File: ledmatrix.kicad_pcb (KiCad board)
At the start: 4 copper layers, 49.8 x 83.2 mm, 86 parts, among them J1 Conn_02x06_Odd_Even, J2 Conn_02x06_Odd_Even, J3 Conn_01x02, Q1 BSS84, Q2 BSS84, Q3 BSS84, Q4 BSS84, Q5 BSS84, Q6 BSS84, Q7 BSS84, Q8 BSS84, U1 mbi5029gd, U2 74HC137

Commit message: nicefy
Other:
- board text added: "'HC137 (rows)"
- board text added: "A -- K green A -- K red"
- board text added: "A1 A0 ~{E1} A2 CLK LE ~{OE} DIN ⏚ ⏚ 5V 5V"
- board text added: "A1 A0 ~{E1} A2 CLK LE ~{OE} DOUT ⏚ ⏚ 5V 5V"
- board text added: "green = col 14 ↑ red = col 15 ↑"
- board text added: "mbi5029gd (cols)"
- board text added: "↑ green = col 0 ↑ red = col 1"
- board text added: "↓ row 0 ↓"
- board text added: "↓ row 7 ↓"
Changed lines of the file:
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@@
   (net 42 "/A6")
   (net 43 "/A7")
-  (net 44 "Net-(U1-Pad23)")
+  (net 44 "Net-(R1-Pad2)")
   (footprint "panasonic_led_ln2162c68:LN2162C68" (layer "F.Cu")
     (at 90.17 95.25)
@@
       (net 18 "+5V") (pintype "passive"))
     (pad "2" smd roundrect locked (at 0.825 0 90) (size 0.8 0.95) (layers "F.Cu" "F.Paste" "F.Mask") (roundrect_rratio 0.25)
-      (net 44 "Net-(U1-Pad23)") (pintype "passive"))
+      (net 44 "Net-(R1-Pad2)") (pintype "passive"))
     (model "${KICAD6_3DMODEL_DIR}/Resistor_SMD.3dshapes/R_0603_1608Metric.wrl"
       (offset (xyz 0 0 0))
@@
       (net 35 "/DOUT") (pinfunction "SDO") (pintype "output"))
     (pad "23" smd roundrect locked (at 4.65 -5.715 90) (size 2.05 0.6) (layers "F.Cu" "F.Paste" "F.Mask") (roundrect_rratio 0.25)
-      (net 44 "Net-(U1-Pad23)") (pinfunction "R-EXT") (pintype "passive"))
+      (net 44 "Net-(R1-Pad2)") (pinfunction "R-EXT") (pintype "passive"))
     (pad "24" smd roundrect locked (at 4.65 -6.985 90) (size 2.05 0.6) (layers "F.Cu" "F.Paste" "F.Mask") (roundrect_rratio 0.25)
       (net 18 "+5V") (pinfunction "VDD") (pintype "power_in"))
@@
     (property "Sheetname" "")
     (attr smd)
-    (fp_text reference "C1" (at 1.905 -3.048 180) (layer "F.SilkS")
+    (fp_text reference "C1" (at 2.286 1.524 180) (layer "F.SilkS")
       (effects (font (size 0.75 0.75) (thickness 0.1)))
     )
@@
     (fp_line (start -1.93 -8.4) (end -3.13 -8.4) (layer "B.Fab") (width 0.1))
     (pad "1" thru_hole roundrect locked (at 0 0 180) (size 1.7 1.7) (drill 1) (layers *.Cu *.Mask) (roundrect_rratio 0.1470588235)
-      (net 26 "/ROW_A0") (pinfunction "Pin_1") (pintype "passive"))
+      (net 26 "/ROW_A0") (pinfunction "Pin_1"))
     (pad "2" thru_hole circle locked (at 2.54 0 180) (size 1.7 1.7) (drill 1) (layers *.Cu *.Mask)
-      (net 31 "/ROW_A1") (pinfunction "Pin_2") (pintype "passive"))
+      (net 31 "/ROW_A1") (pinfunction "Pin_2"))
     (pad "3" thru_hole circle locked (at 0 -2.54 180) (size 1.7 1.7) (drill 1) (layers *.Cu *.Mask)
-      (net 27 "/ROW_A2") (pinfunction "Pin_3") (pintype "passive"))
+      (net 27 "/ROW_A2") (pinfunction "Pin_3"))
     (pad "4" thru_hole circle locked (at 2.54 -2.54 180) (size 1.7 1.7) (drill 1) (layers *.Cu *.Mask)
-      (net 32 "/ROW_~{E1}") (pinfunction "Pin_4") (pintype "passive"))
+      (net 32 "/ROW_~{E1}") (pinfunction "Pin_4"))
     (pad "5" thru_hole circle locked (at 0 -5.08 180) (size 1.7 1.7) (drill 1) (layers *.Cu *.Mask)
-      (net 28 "/LE{slash}MOD{slash}CA") (pinfunction "Pin_5") (pintype "passive"))
+      (net 28 "/LE{slash}MOD{slash}CA") (pinfunction "Pin_5"))
     (pad "6" thru_hole circle locked (at 2.54 -5.08 180) (size 1.7 1.7) (drill 1) (layers *.Cu *.Mask)
-      (net 33 "/CLK") (pinfunction "Pin_6") (pintype "passive"))
+      (net 33 "/CLK") (pinfunction "Pin_6"))
     (pad "7" thru_hole circle locked (at 0 -7.62 180) (size 1.7 1.7) (drill 1) (layers *.Cu *.Mask)
-      (net 29 "/DIN") (pinfunction "Pin_7") (pintype "passive"))
+      (net 29 "/DIN") (pinfunction "Pin_7"))
     (pad "8" thru_hole circle locked (at 2.54 -7.62 180) (size 1.7 1.7) (drill 1) (layers *.Cu *.Mask)
-      (net 34 "/~{OE}{slash}SW{slash}~{ED}") (pinfunction "Pin_8") (pintype "passive"))
+      (net 34 "/~{OE}{slash}SW{slash}~{ED}") (pinfunction "Pin_8"))
     (pad "9" thru_hole circle locked (at 0 -10.16 180) (size 1.7 1.7) (drill 1) (layers *.Cu *.Mask)
-      (net 30 "GND") (pinfunction "Pin_9") (pintype "passive"))
+      (net 30 "GND") (pinfunction "Pin_9"))
     (pad "10" thru_hole circle locked (at 2.54 -10.16 180) (size 1.7 1.7) (drill 1) (layers *.Cu *.Mask)
-      (net 30 "GND") (pinfunction "Pin_10") (pintype "passive"))
+      (net 30 "GND") (pinfunction "Pin_10"))
     (pad "11" thru_hole circle locked (at 0 -12.7 180) (size 1.7 1.7) (drill 1) (layers *.Cu *.Mask)
-      (net 18 "+5V") (pinfunction "Pin_11") (pintype "passive"))
+      (net 18 "+5V") (pinfunction "Pin_11"))
     (pad "12" thru_hole circle locked (at 2.54 -12.7 180) (size 1.7 1.7) (drill 1) (layers *.Cu *.Mask)
-      (net 18 "+5V") (pinfunction "Pin_12") (pintype "passive"))
+      (net 18 "+5V") (pinfunction "Pin_12"))
     (model "${KICAD6_3DMODEL_DIR}/Connector_IDC.3dshapes/IDC-Header_2x06_P2.54mm_Latch_Vertical.wrl"
       (offset (xyz 0 0 0))
@@
     )
   )
+  (gr_line (start 91.186 25.908) (end 90.932 26.162) (layer "F.SilkS") (width 0.127))
+  (gr_line (start 90.932 24.511) (end 90.678 24.511) (layer "F.SilkS") (width 0.127))
+  (gr_line (start 91.186 23.876) (end 90.932 24.13) (layer "F.SilkS") (width 0.127))
+  (gr_line (start 90.932 25.654) (end 91.186 25.908) (layer "F.SilkS") (width 0.127))
+  (gr_line (start 90.932 22.86) (end 90.932 23.622) (layer "F.SilkS") (width 0.127))
+  (gr_line (start 90.932 23.622) (end 91.186 23.876) (layer "F.SilkS") (width 0.127))
+  (gr_line (start 90.932 24.13) (end 90.932 24.511) (layer "F.SilkS") (width 0.127))
+  (gr_line (start 90.932 27.178) (end 90.678 27.178) (layer "F.SilkS") (width 0.127))
+  (gr_line (start 90.932 26.162) (end 90.932 27.178) (layer "F.SilkS") (width 0.127))
+  (gr_line (start 90.678 22.86) (end 90.932 22.86) (layer "F.SilkS") (width 0.127))
+  (gr_line (start 90.678 24.892) (end 90.932 24.892) (layer "F.SilkS") (width 0.127))
+  (gr_line (start 90.932 24.892) (end 90.932 25.654) (layer "F.SilkS") (width 0.127))
   (gr_line (start 118.245 104.267) (end 68.445 104.267) (layer "Edge.Cuts") (width 0.1))
   (gr_line (start 68.445 104.267) (end 68.445 21.082) (layer "Edge.Cuts") (width 0.1))
   (gr_line (start 118.245 21.082) (end 118.245 104.267) (layer "Edge.Cuts") (width 0.1))
   (gr_line (start 118.245 21.082) (end 68.445 21.082) (layer "Edge.Cuts") (width 0.1))
+  (gr_text "↓ row 0 ↓" (at 83.82 54.356) (layer "F.SilkS")
+    (effects (font (size 0.75 0.75) (thickness 0.1)))
+  )
+  (gr_text "'HC137\n(rows)" (at 94.488 23.876) (layer "F.SilkS")
+    (effects (font (size 0.75 0.75) (thickness 0.1)))
+  )
+  (gr_text "↑ green = col 0\n↑ red = col 1" (at 70.612 66.548) (layer "F.SilkS")
+    (effects (font (size 0.75 0.75) (thickness 0.1)) (justify left))
+  )
+  (gr_text "mbi5029gd\n(cols)" (at 94.488 26.924) (layer "F.SilkS")
+    (effects (font (size 0.75 0.75) (thickness 0.1)))
+  )
+  (gr_text "green = col 14 ↑\nred = col 15 ↑" (at 115.57 66.548) (layer "F.SilkS")
+    (effects (font (size 0.75 0.75) (thickness 0.1)) (justify right))
+  )
+  (gr_text "A1 A0\n~{E1} A2\nCLK LE\n~{OE} DOUT\n⏚ ⏚\n5V 5V" (at 87.63 26.162) (layer "F.SilkS")
+    (effects (font (size 0.75 0.75) (thickness 0.1)))
+  )
+  (gr_text "↓ row 7 ↓" (at 83.82 98.552) (layer "F.SilkS")
+    (effects (font (size 0.75 0.75) (thickness 0.1)))
+  )
+  (gr_text "A -- K green\nA -- K red" (at 94.234 60.325) (layer "F.SilkS")
+    (effects (font (size 0.75 0.75) (thickness 0.1)) (justify left))
+  )
+  (gr_text "A1 A0\n~{E1} A2\nCLK LE\n~{OE} DIN\n⏚ ⏚\n5V 5V" (at 74.93 26.162) (layer "F.SilkS")
+    (effects (font (size 0.75 0.75) (thickness 0.1)))
+  )
   (segment (start 105.41 52.578) (end 105.664 52.324) (width 0.127) (layer "F.Cu") (net 1))
   (segment (start 72.82 59.612) (end 72.82 62.6) (width 0.127) (layer "F.Cu") (net 1))

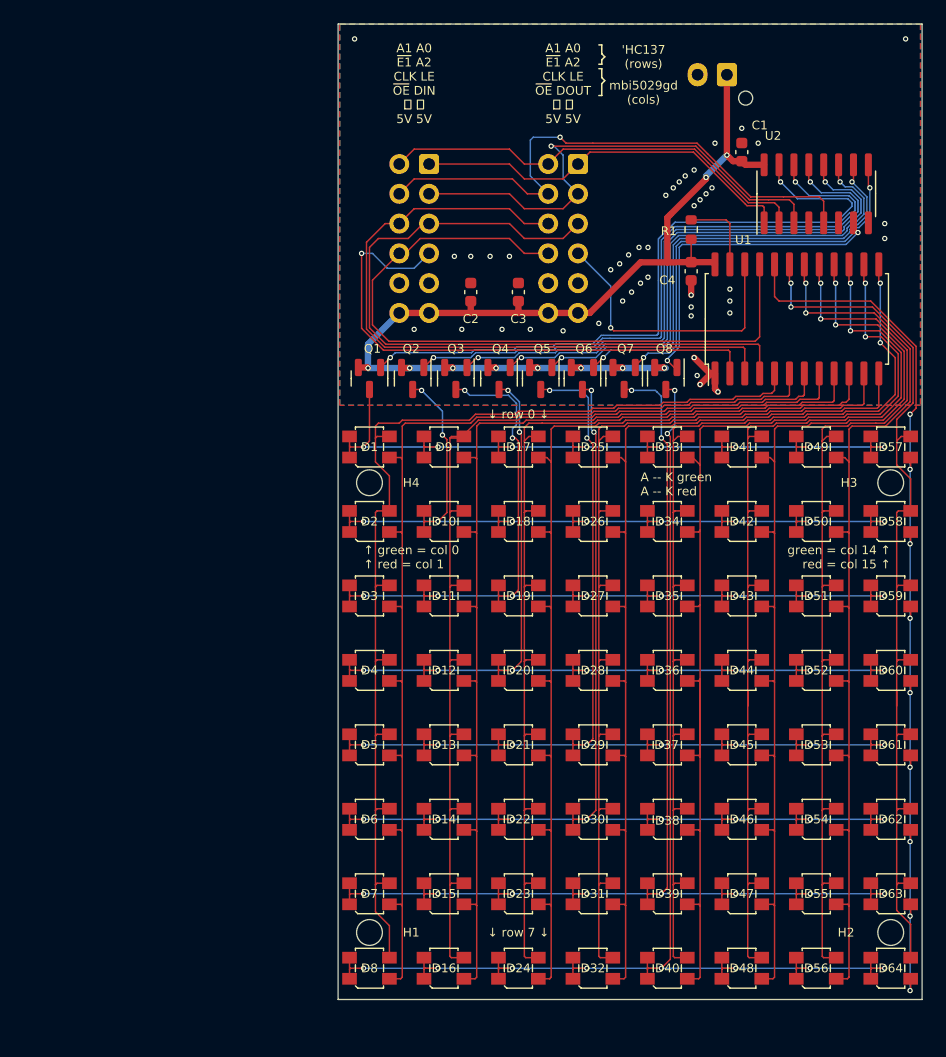
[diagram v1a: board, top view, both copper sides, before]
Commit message: changes, mostly adapting to proper JLCpcb 4layer rules
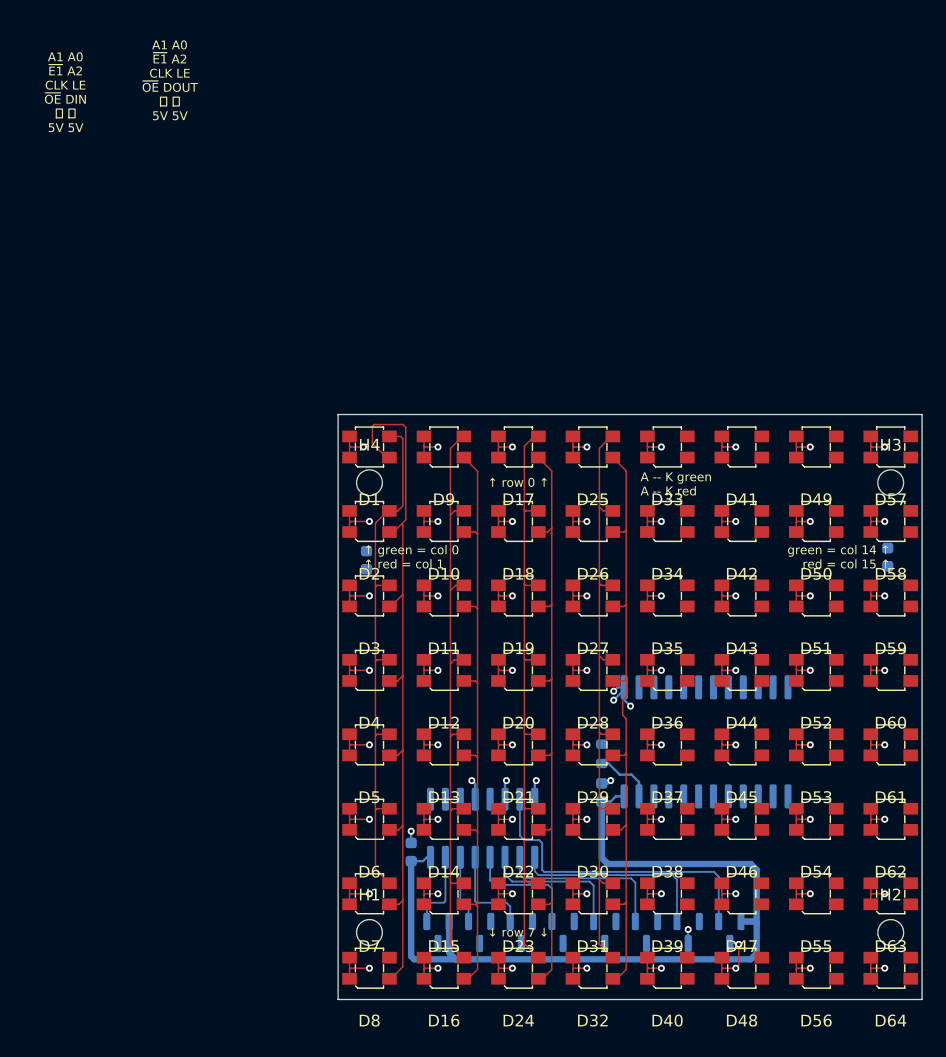
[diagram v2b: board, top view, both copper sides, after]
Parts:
- removed J1, J2: Conn_02x06_Odd_Even, Connector_IDC:IDC-Header_2x06_P2.54mm_Latch_Vertical
- removed J3: Conn_01x02, Connector_JST:JST_XH_B2B-XH-AM_1x02_P2.50mm_Vertical
- C1, C2, C3, C4, Q1, Q2, Q3, Q4, Q5, Q6, Q7, Q8, R1, U1, U2: moved to B.Cu
- moved C1 66.0 mm to (74.7, 91.7)
- moved U2 61.1 mm to (80.8, 89.7), turned to -90 degrees
- moved Q1 47.6 mm to (77.0, 98.6)
- moved Q2 47.6 mm to (80.5, 98.6)
- moved Q3 47.6 mm to (84.1, 98.6)
- moved Q4 47.6 mm to (87.6, 98.6)
- moved Q5 47.6 mm to (91.2, 98.6)
- moved Q6 47.6 mm to (94.7, 98.6)
- moved Q7 47.6 mm to (98.3, 98.6)
- moved Q8 47.6 mm to (101.9, 98.6)
- moved R1 45.3 mm to (90.9, 83.3), turned to -90 degrees
- moved C4 45.1 mm to (90.9, 86.6), turned to 90 degrees
- moved C2 42.1 mm to (115.3, 66.5)
- moved U1 36.9 mm to (99.8, 82.3), turned to -90 degrees
- moved C3 26.3 mm to (70.9, 66.8)
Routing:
- net /LED Matrix/K9: track 94.0 -> 0.00 mm, vias 2 -> 0
- net /LED Matrix/K8: track 86.9 -> 0.00 mm, vias 2 -> 0
- net /LED Matrix/K10: track 84.9 -> 0.00 mm, vias 2 -> 0
- net /LED Matrix/K11: track 84.2 -> 0.00 mm, vias 2 -> 0
- net /LED Matrix/K13: track 81.0 -> 0.00 mm, vias 2 -> 0
- net /LED Matrix/K12: track 80.8 -> 0.00 mm, vias 2 -> 0
- net /LED Matrix/K15: track 79.9 -> 0.00 mm, vias 9 -> 0
- net /LED Matrix/K14: track 79.0 -> 0.00 mm, vias 2 -> 0
- net /LE/MOD/CA: track 62.8 -> 0.00 mm
- net /~{OE}/SW/~{ED}: track 60.7 -> 0.00 mm
- net /CLK: track 59.7 -> 0.00 mm
- net /G0: track 59.3 -> 6.88 mm, vias 2 -> 0
- net /G1: track 55.3 -> 5.92 mm, vias 2 -> 0
- net /ROW_~{E1}: track 48.2 -> 0.00 mm, vias 1 -> 0
- net /A7: track 119.4 -> 71.6 mm, vias 10 -> 9
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- added copper zone on In2.Cu, net GND
- removed copper zone on B.Cu, net GND
- removed copper zone on F.Cu, net GND
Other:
- board size 49.8 x 83.2 mm -> 49.8 x 49.9 mm
- rule pad_to_mask_clearance: 0.0381 -> 0.2
- board text added: "↑ row 0 ↑"
- board text removed: "'HC137 (rows)"
- board text removed: "mbi5029gd (cols)"
- board text removed: "↓ row 0 ↓"
